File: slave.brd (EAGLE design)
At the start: 221.8 x 119.2 mm, 321 parts, among them J2 EB21A-06-D, J3 EB21A-06-D, J4 EB21A-06-D, J5 EB21A-06-D, J6 282837-9, J7 282837-9, J8 282837-9, J9 1715250000, Q1 DMN2056U-7, Q10 DMN2056U-7, Q11 DMN2056U-7, Q12 DMN2056U-7, Q13 DMN2056U-7, Q14 DMN2056U-7, Q15 DMN2056U-7, Q16 DMN2056U-7, Q17 DMN2056U-7, Q18 DMN2056U-7, Q19 DMN2056U-7, Q2 DMN2056U-7, Q20 DMN2056U-7, Q21 DMN2056U-7, Q22 DMN2056U-7, Q23 DMN2056U-7, Q24 DMN2056U-7, Q25 DMN2056U-7, Q26 DMN2056U-7, Q27 DMN2056U-7, Q28 DMN2056U-7, Q29 DMN2056U-7, Q3 DMN2056U-7, Q30 DMN2056U-7, Q31 DMN2056U-7, Q32 DMN2056U-7, Q33 DMN2056U-7, Q34 DMN2056U-7, Q35 DMN2056U-7, Q36 DMN2056U-7, Q37 DMN2056U-7, Q38 DMN2056U-7, Q39 DMN2056U-7, Q4 DMN2056U-7, Q40 DMN2056U-7, Q41 DMN2056U-7, Q42 DMN2056U-7, Q5 DMN2056U-7, Q7 DMN2056U-7, Q8 DMN2056U-7, Q9 DMN2056U-7, U2 AP2112K-3.3TRG1, U3 MCP23008-E/P, U4 MCP23008-E/P, U5 MCP23008-E/P, U6 MC74HCT4851ADR2G, U7 MC74HCT4851ADR2G, U8 MC74HCT4851ADR2G, U9 MC74HCT4851ADR2G

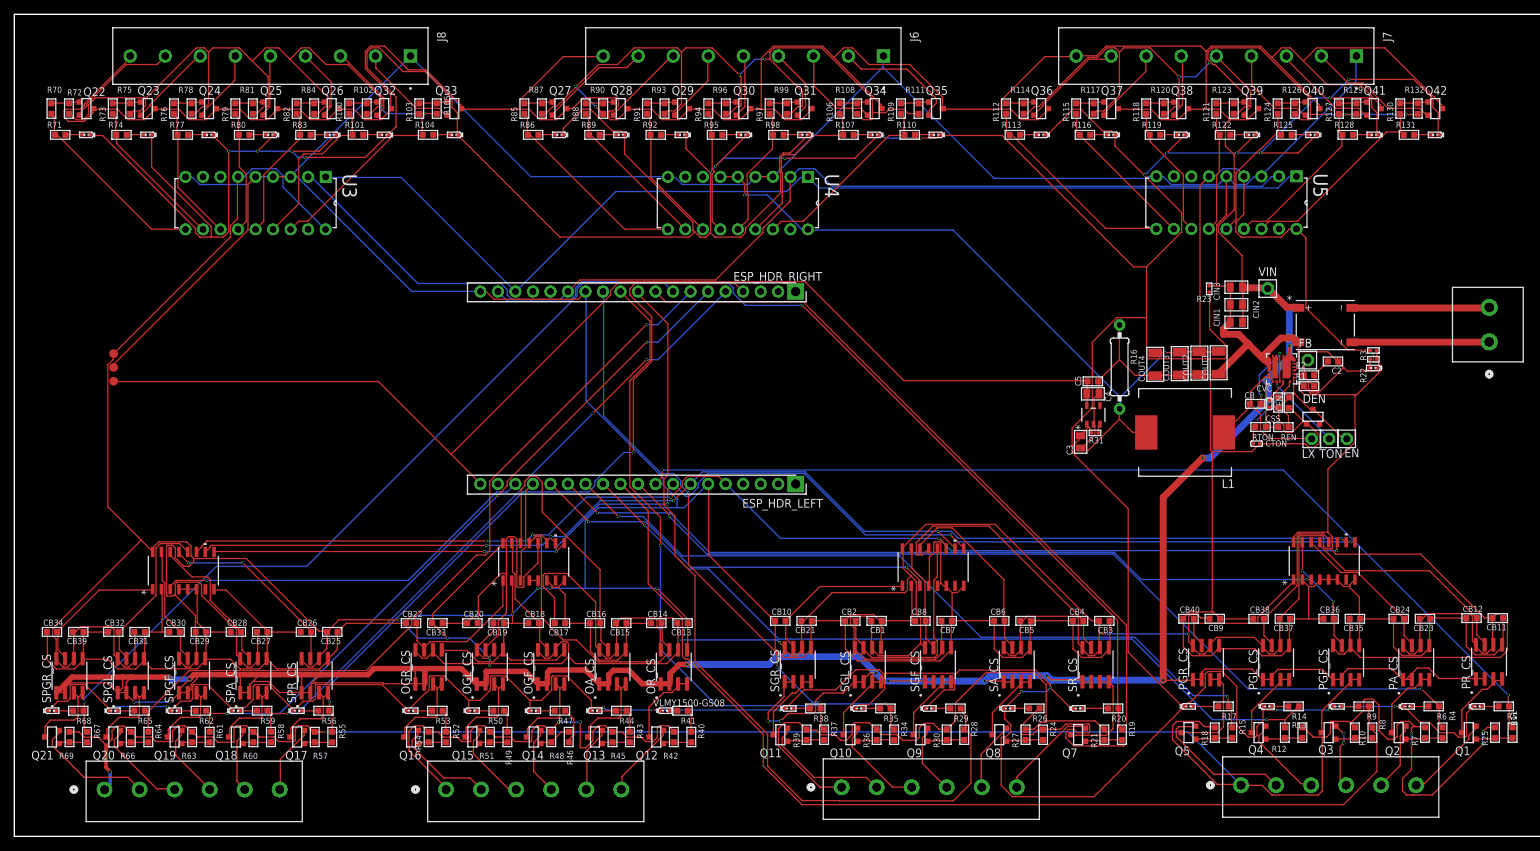
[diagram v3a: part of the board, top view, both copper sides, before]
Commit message: fixed GND labels for individual ports and FETs, rerouted. Fixed GND thickness in MOS sides, Put labels, Combined overhead and primary esp pin nets
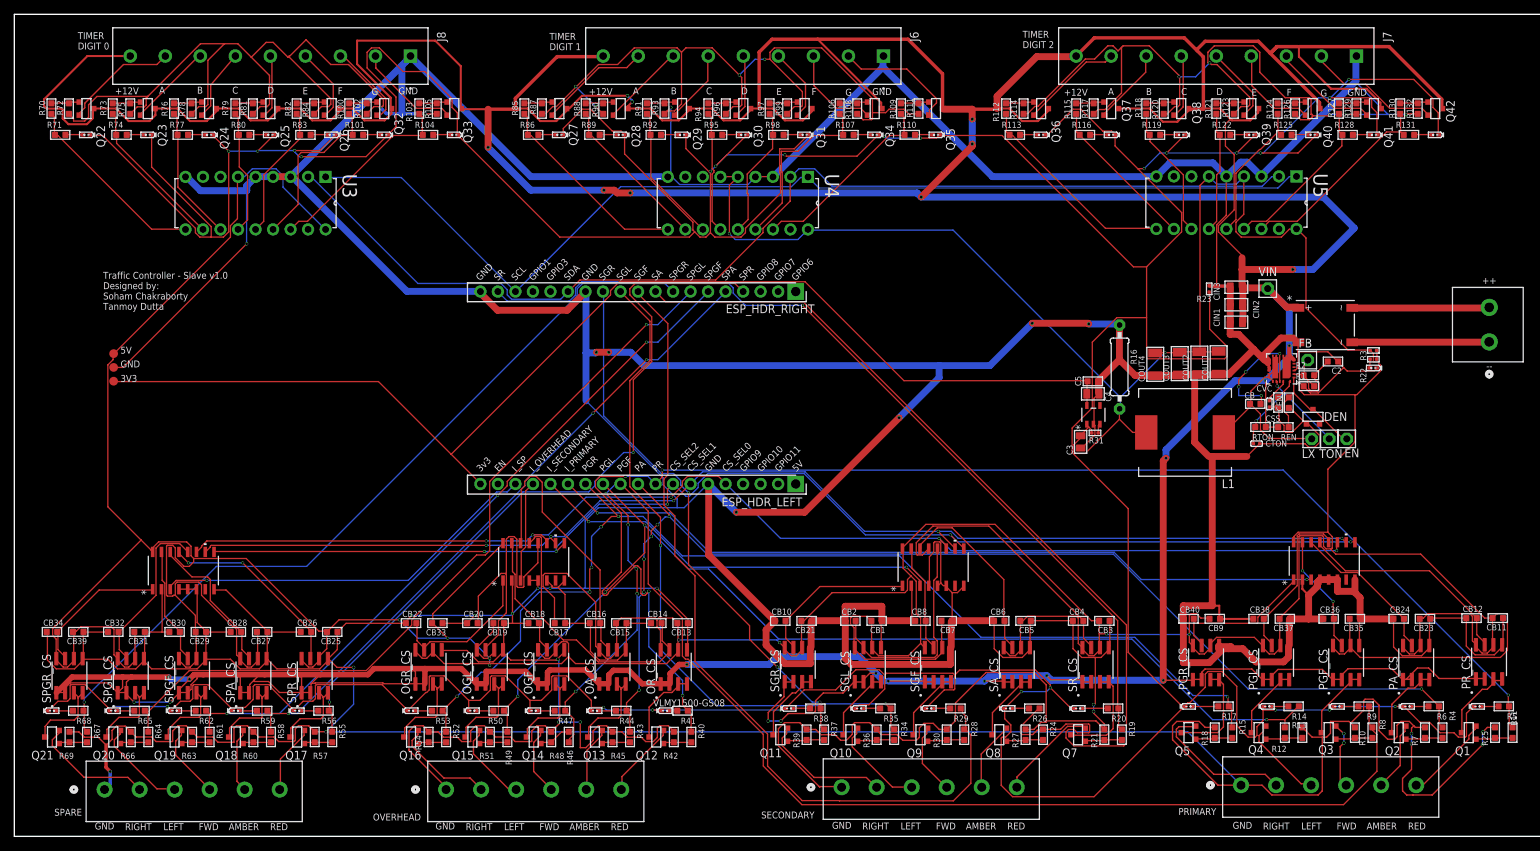
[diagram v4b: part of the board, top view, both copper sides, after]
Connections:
- removed net D0_GND: R102.1, R105.1, R72.1, R75.1, R78.1, R81.1, R84.1
- removed net D1_GND: R108.1, R111.1, R87.1, R90.1, R93.1, R96.1, R99.1
- removed net D2_GND: R114.1, R117.1, R120.1, R123.1, R126.1, R129.1, R132.1
- removed net OA: R43.2, R44.2
- removed net OGF: R46.2, R47.2
- removed net OGL: R49.2, R50.2
- removed net OGR: R52.2, R53.2
- removed net OLED_GND: J4.1, R42.1, R45.1, R48.1, R51.1, R54.1
- removed net OR: R40.2, R41.2
- removed net PLED_GND: J2.1, J5.1, R10.1, R14.1, R18.1, R25.1, R57.1, R60.1, R63.1, R66.1, R69.1, R7.1
- removed net SLED_GND: J3.1, R21.1, R27.1, R30.1, R36.1, R39.1
- net GND: now also J2.1, J3.1, J4.1, J5.1, R10.1, R102.1, R105.1, R108.1, R111.1, R114.1, R117.1, R120.1, R123.1, R126.1, R129.1, R132.1, R14.1, R18.1, R21.1, R25.1, R27.1, R30.1, R36.1, R39.1, R42.1, R45.1, R48.1, R51.1, R54.1, R57.1, R60.1, R63.1, R66.1, R69.1, R7.1, R72.1, R75.1, R78.1, R81.1, R84.1, R87.1, R90.1, R93.1, R96.1, R99.1
- net PA: now also R43.2, R44.2
- net PGF: now also R46.2, R47.2
- net PGL: now also R49.2, R50.2
- net PGR: now also R52.2, R53.2
- net PR: now also R40.2, R41.2
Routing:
- net GND: track 1052.2 -> 2036.8 mm, vias 6 -> 37
- net PLED_GND: track 293.3 -> 0.00 mm, vias 6 -> 0
- net VIN: track 849.6 -> 1050.7 mm, vias 15 -> 24
- net D1_GND: track 107.0 -> 0.00 mm, vias 4 -> 0
- net D2_GND: track 106.3 -> 0.00 mm, vias 5 -> 0
- net D0_GND: track 106.1 -> 0.00 mm, vias 2 -> 0
- net SLED_GND: track 83.0 -> 0.00 mm
- net OLED_GND: track 65.5 -> 0.00 mm, vias 2 -> 0
- net PR: track 143.5 -> 207.8 mm, vias 2 -> 5
- net PGR: track 110.6 -> 158.2 mm, vias 2 -> 6
- net PGF: track 152.9 -> 198.7 mm, vias 0 -> 5
- net PGL: track 117.0 -> 155.6 mm, vias 2 -> 4
- net PA: track 132.9 -> 167.3 mm, vias 2 -> 7
- net +5V: track 951.1 -> 957.9 mm
- net BST: track 12.8 -> 18.7 mm, vias 2 -> 4
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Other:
- board text added: "++"
- board text added: "+12V"
- board text added: "--"
- board text added: "3V3"
- board text added: "3v3"
- board text added: "5V"
- board text added: "A"
- board text added: "AMBER"
- board text added: "B"
- board text added: "C"
- board text added: "CS_SEL0"
- board text added: "CS_SEL1"
- board text added: "CS_SEL2"
- board text added: "D"
- board text added: "E"
- board text added: "EN"
- board text added: "F"
- board text added: "FWD"
- board text added: "G"
- board text added: "GND"
- board text added: "GPIO1"
- board text added: "GPIO10"
- board text added: "GPIO11"
- board text added: "GPIO3"
- board text added: "GPIO6"
- board text added: "GPIO7"
- board text added: "GPIO8"
- board text added: "GPIO9"
- board text added: "I_OVERHEAD"
- board text added: "I_PRIMARY"
- board text added: "I_SECONDARY"
- board text added: "I_SP"
- board text added: "LEFT"
- board text added: "OVERHEAD"
- board text added: "PA"
- board text added: "PGF"
- board text added: "PGL"
- board text added: "PGR"
- board text added: "PR"
- board text added: "PRIMARY"
- board text added: "RED"
- board text added: "RIGHT"
- board text added: "SA"
- board text added: "SCL"
- board text added: "SDA"
- board text added: "SECONDARY"
- board text added: "SGF"
- board text added: "SGL"
- board text added: "SGR"
- board text added: "SPA"
- board text added: "SPARE"
- board text added: "SPGF"
- board text added: "SPGL"
- board text added: "SPGR"
- board text added: "SPR"
- board text added: "SR"
- board text added: "TIMER DIGIT 0"
- board text added: "TIMER DIGIT 1"
- board text added: "TIMER DIGIT 2"
- board text added: "Traffic Controller - Slave v1.0 Designed by: Soham Chakraborty Tanmoy Dutta"
